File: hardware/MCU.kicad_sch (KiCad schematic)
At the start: 57 parts, among them SW2 SW_Push, SW3 SW_Push, U6 W25N02KVZEIR, Y1 Crystal, Y2 24MHz

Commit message: feat(Hw):Update_Schematic_And_BOM
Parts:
- added J2: Conn_01x04_Pin, Connector_PinHeader_2.54mm:PinHeader_1x04_P2.54mm_Vertical, symbol Connector:Conn_01x04_Pin
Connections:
- net +3V3: now also J2.4 (Pin_4)
- net DEBUG_RX: now also J2.2 (Pin_2)
- net DEBUG_TX: now also J2.3 (Pin_3)
- net GND: now also J2.1 (Pin_1)
- net CODEC_LINEOUT: no longer names the net of U8.29 (CODEC_LINEOUT)
- net CODEC_MIC0N: no longer names the net of U8.33 (CODEC_MIC0N)
- net CODEC_MIC0P: no longer names the net of U8.34 (CODEC_MIC0P)
- net CODEC_MIC1N: no longer names the net of U8.35 (CODEC_MIC1N)
- net CODEC_MIC1P: no longer names the net of U8.36 (CODEC_MIC1P)
- net CODEC_MICBIAS: no longer names the net of U8.32 (CODEC_MICBIAS)
- net CODEC_VCM: no longer names the net of C1.1, U8.30 (CODEC_VCM)
- net ETH_AVDD3V3: no longer names the net of R29.2, U8.101 (ETH_AVDD3V3)
- net ETH_PHY_RXN: no longer names the net of U8.97 (ETH_PHY_RXN)
- net ETH_PHY_RXP: no longer names the net of U8.98 (ETH_PHY_RXP)
- net ETH_PHY_TXN: no longer names the net of U8.99 (ETH_PHY_TXN)
- net ETH_PHY_TXP: no longer names the net of U8.100 (ETH_PHY_TXP)
- net GPIO0_A0_Z: no longer names the net of U8.58 (UART0_RX_M0/CLK_32K/CLK_REFOUT/RTC_CLKO/GPIO0_A0_Z)
- net GPIO0_A1_D: no longer names the net of U8.59 (UART0_TX_M0/PWM2_M0/GPIO0_A1_D)
- net GPIO0_A2_D: no longer names the net of U8.60 (PWM3_IR_M0/GPIO0_A2_D)
- net GPIO0_A3_U: no longer names the net of U8.62 (PMIC_PWR_CTRL_M1/GPIO0_A3_U)
- net GPIO0_A4_D: no longer names the net of U8.63 (PMIC_PWR_CTRL_M0/PWM1_M0/GPIO0_A4_D)
- net GPIO0_A5_D: no longer names the net of U8.64 (I2C1_SCL_M0/UART1_RTS_M0/PWM5_M0/GPIO0_A5_D)
- net GPIO0_A6_D: no longer names the net of U8.65 (I2C1_SDA_M0/UART1_CTS_M0/PWM6_M0/GPIO0_A6_D)
- net GPIO1_A2_D: no longer names the net of U8.74 (PWM0_M0/CPU_AVS/VI_CIF_D0_M1/GPIO1_A2_D)
- net GPIO1_A3_D: no longer names the net of U8.75 (UART1_TX_M0/I2C0_SCL_M0/GPIO1_A3_D)
- net GPIO1_A4_D: no longer names the net of U8.76 (UART1_RX_M0/I2C0_SDA_M0/GPIO1_A4_D)
- net GPIO1_B0_D: no longer names the net of U8.77 (UART4_RX_M0/PWM3_IR_M1/GPIO1_B0_D)
- net GPIO1_C1_D: no longer names the net of U8.94 (VO_LCDC_D6/VI_CIF_D3_M1/PWM4_M2/SPI0_CLK_M0/_SDMMC1_D0_M1/GPIO1_C1_D)
- net GPIO1_C3_D: no longer names the net of U8.92 (VO_LCDC_D4/VI_CIF_D5_M1/PWM6_M2/I2C4_SDA_M1/_SDMMC1_CMD_M1/SPI0_MISO_M0/GPIO1_C3_D)
- net GPIO1_C4_D: no longer names the net of U8.91 (VO_LCDC_D3/VI_CIF_D6_M1/PWM8_M1/UART4_RX_M1_/SDMMC1_D3_M1/GPIO1_C4_D)
- net GPIO1_C5_D: no longer names the net of U8.90 (VO_LCDC_D2/VI_CIF_D7_M1/PWM9_M1/UART4_TX_M1/_SDMMC1_D2_M1/GPIO1_C5_D)
- net GPIO1_C6_D: no longer names the net of U8.83 (VO_LCDC_D1/VI_CIF_D8_M1/PWM10_M1/UART4_RTS__M1/GPIO1_C6_D)
- net GPIO1_C7_D: no longer names the net of U8.84 (VO_LCDC_D0/VI_CIF_D9_M1/PWM11_IR_M1/UART4_CT_S_M1/GPIO1_C7_D)
- net GPIO1_D0_D: no longer names the net of U8.89 (VO_LCDC_DEN/VI_CIF_CLKI_M1/PWM3_IR_M2/UART5__RTS_M1/UART3_TX_M1/GPIO1_D0_D)
- net GPIO1_D1_D: no longer names the net of U8.87 (VO_LCDC_HSYNC/VI_CIF_HREF_M1/PWM10_M2/UART5__CTS_M1/UART3_RX_M1/GPIO1_D1_D)
- net GPIO1_D2_D: no longer names the net of U8.86 (VO_LCDC_VSYNC/VI_CIF_VSYNC_M1/I2C3_SDA_M1/UA_RT5_RX_M1/SPI0_CS1_M0/PWM0_M1/AUD_DSM_P/GPI_O1_D2_D)
- net GPIO1_D3_D: no longer names the net of U8.85 (VO_LCDC_CLK/VI_CIF_CLKO_M1/I2C3_SCL_M1/UART5__TX_M1/PWM11_IR_M2/AUD_DSM_N/GPIO1_D3_D)
- net GPIO2_A0_D_1: no longer names the net of U8.109 (SDMMC1_D1_M0/I2S0_SCLK/VO_LCDC_D8/UART1_CTS__M1/I2C4_SDA_M0/GPIO2_A0_D_1)
- net GPIO2_A0_D_2: no longer names the net of U8.110 (SDMMC1_D1_M0/I2S0_SCLK/VO_LCDC_D8/UART1_CTS__M1/I2C4_SDA_M0/GPIO2_A0_D_2)
- net GPIO2_A3_D: no longer names the net of U8.112 (SDMMC1_CMD_M0/I2S0_SDO3_SDI1/VO_LCDC_D11/GP_IO2_A3_D)
- net GPIO2_A4_D: no longer names the net of U8.113 (SDMMC1_D3_M0/I2S0_SDO0/VO_LCDC_D12/UART1_TX__M1/GPIO2_A4_D)
- net GPIO2_A5_D: no longer names the net of U8.114 (SDMMC1_D2_M0/I2S0_SDI0/VO_LCDC_D13/UART1_RX__M1/GPIO2_A5_D)
- net GPIO2_A6_D: no longer names the net of U8.107 (UART0_RTS_M1/I2S0_SDO2_SDI2/VO_LCDC_D14/PWM_2_M1/I2C3_SCL_M0/FLASH_TRIG_OUT/GPIO2_A6_D)
- net GPIO2_A7_D: no longer names the net of U8.106 (UART0_CTS_M1/I2S0_SDO1_SDI3/VO_LCDC_D15/PWM_4_M1/I2C3_SDA_M0/PRELIGHT_TRIG_OUT/GPIO2_A7_D)
- net GPIO2_A_2_D: no longer names the net of U8.111 (SDMMC1_CLK_M0/I2S0_MCLK/VO_LCDC_D10/GPIO2_A_2_D)
- net GPIO2_B1_D_1: no longer names the net of U8.104 (UART0_TX_M1/I2C1_SDA_M1/VO_LCDC_D17/PWM6_M1_/GPIO2_B1_D_1)
- net GPIO2_B1_D_2: no longer names the net of U8.105 (UART0_TX_M1/I2C1_SDA_M1/VO_LCDC_D17/PWM6_M1_/GPIO2_B1_D_2)
- net GPIO3_A3_U: no longer names the net of U8.14 (SDMMC0_D0/UART2_RX_M0/PWM8_M0/GPIO3_A3_U)
- net GPIO3_A4_D: no longer names the net of U8.15 (SDMMC0_CLK/UART5_RTS_M0/I2C0_SCL_M2/JTAG_LPMCU_TC_K_M1/PWM10_M0/GPIO3_A4_D)
- net GPIO3_A5_U: no longer names the net of U8.16 (SDMMC0_CMD/UART5_CTS_M0/I2C0_SDA_M2/JTAG_LPMCU_T_MS_M1/PWM11_IR_M0/GPIO3_A5_U)
- net GPIO3_A6_U: no longer names the net of U8.17 (SDMMC0_D3/UART5_TX_M0/JTAG_CPU_TMS_M0/JTAG_HPMCU__TMS_M1/GPIO3_A6_U)
- net GPIO3_A7_U: no longer names the net of U8.18 (SDMMC0_D2/UART5_RX_M0/JTAG_CPU_TCK_M0/JTAG_HPMCU__TCK_M1/GPIO3_A7_U)
- net GPIO3_B0_D: no longer names the net of U8.117 (VI_CIF_D0_M0/MIPI_CSI_RX_D3N/LVDS_RX_D3N/GPIO_3_B0_D)
- net GPIO3_B1_D: no longer names the net of U8.118 (VI_CIF_D1_M0/MIPI_CSI_RX_D3P/LVDS_RX_D3P/GPIO3__B1_D)
- net GPIO3_B2_D: no longer names the net of U8.119 (VI_CIF_D2_M0/MIPI_CSI_RX_CK1N/LVDS_RX_CK1N/GP_IO3_B2_D)
- net GPIO3_B3_D: no longer names the net of U8.120 (VI_CIF_D3_M0/MIPI_CSI_RX_CK1P/LVDS_RX_CK1P/GPI_O3_B3_D)
- net GPIO3_B4_D: no longer names the net of U8.121 (VI_CIF_D4_M0/MIPI_CSI_RX_D2N/LVDS_RX_D2N/GPIO_3_B4_D)
- net GPIO3_B5_D: no longer names the net of U8.122 (VI_CIF_D5_M0/MIPI_CSI_RX_D2P/LVDS_RX_D2P/GPIO3__B5_D)
- net GPIO3_B6_D renamed MCSI_D1N
- net GPIO3_B7_D renamed MCSI_D1P
- net GPIO3_C0_D renamed MCSI_CKN
- net GPIO3_C1_D renamed MCSI_CKP
- net GPIO3_C2_D renamed MCSI_D0N
- net GPIO3_C3_D renamed MCSI_D0P
- net GPIO3_C4_D renamed MCSI_MCLK
- net GPIO3_C5_D renamed MCSI_RST
- net GPIO3_C7_D renamed CSI_SCK
- net GPIO3_D0_D renamed CSI_SDA
- net GPIO3_D1_D: no longer names the net of U8.6 (VI_CIF_D13/UART5_RTS_M2/I2C3_SCL_M2/GPIO3_D1_D)
- net GPIO3_D2_D: no longer names the net of U8.8 (VI_CIF_D14/UART5_CTS_M2/I2C3_SDA_M2/GPIO3_D2_D)
- net GPIO3_D3_D: no longer names the net of U8.9 (VI_CIF_D15/PWM1_M2/GPIO3_D3_D)
- net GPIO4_A0_U: no longer names the net of U8.46 (EMMC_D7/SPI1_MISO_M0/UART0_RX_M2/I2C0_SDA_M1/GPIO_4_A0_U)
- net GPIO4_A1_U: no longer names the net of U8.45 (EMMC_D6/SPI1_MOSI_M0/UART0_TX_M2/I2C0_SCL_M1/GPIO_4_A1_U)
- net GPIO4_A5_U: no longer names the net of U8.40 (EMMC_D4/SPI1_CS0_M0/UART1_TX_M2/I2C2_SDA_M1/GPIO4__A5_U)
- net GPIO4_A7_U: no longer names the net of U8.38 (EMMC_D5/SPI1_CLK_M0/UART1_RX_M2/I2C2_SCL_M1/GPIO4__A7_U)
- no-connect marks 0 -> 59

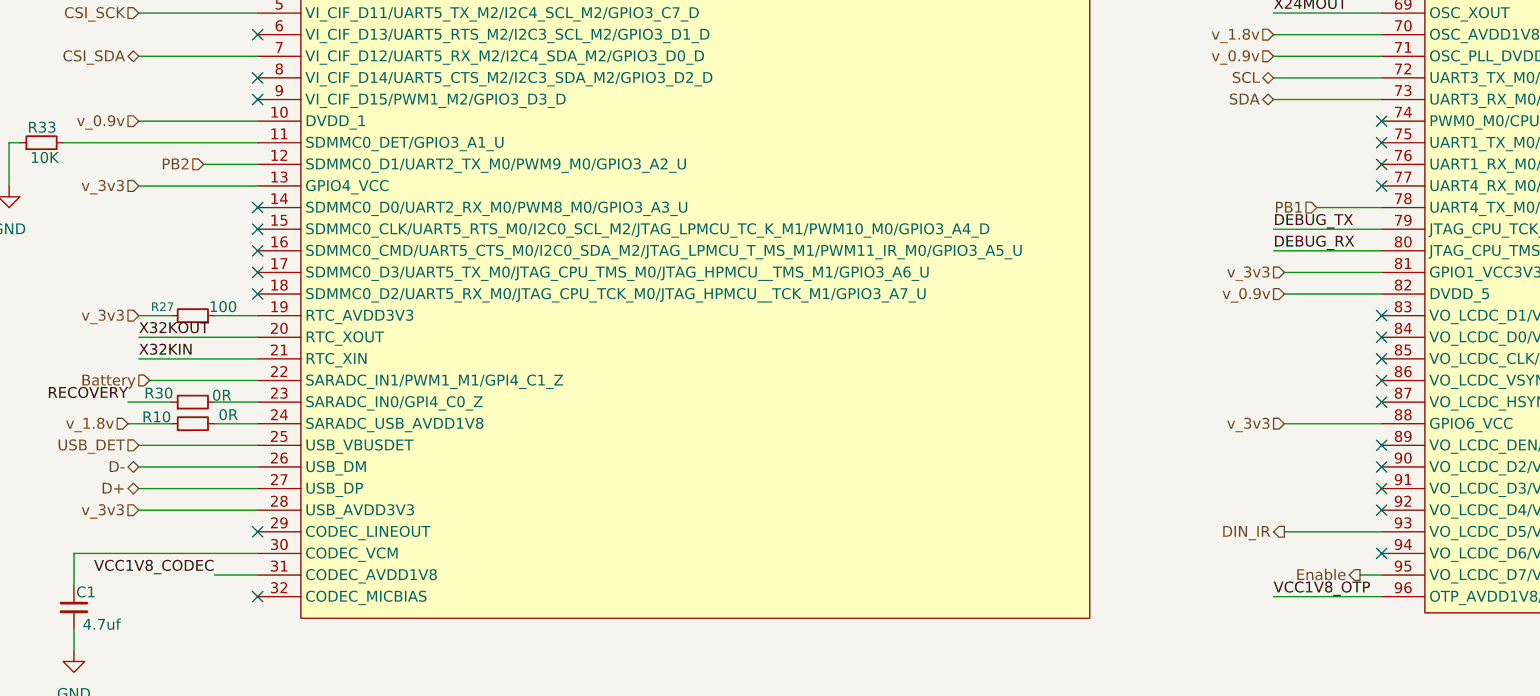
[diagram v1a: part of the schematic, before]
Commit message: feat(Hw):Update_Schematic_And_Floorplan
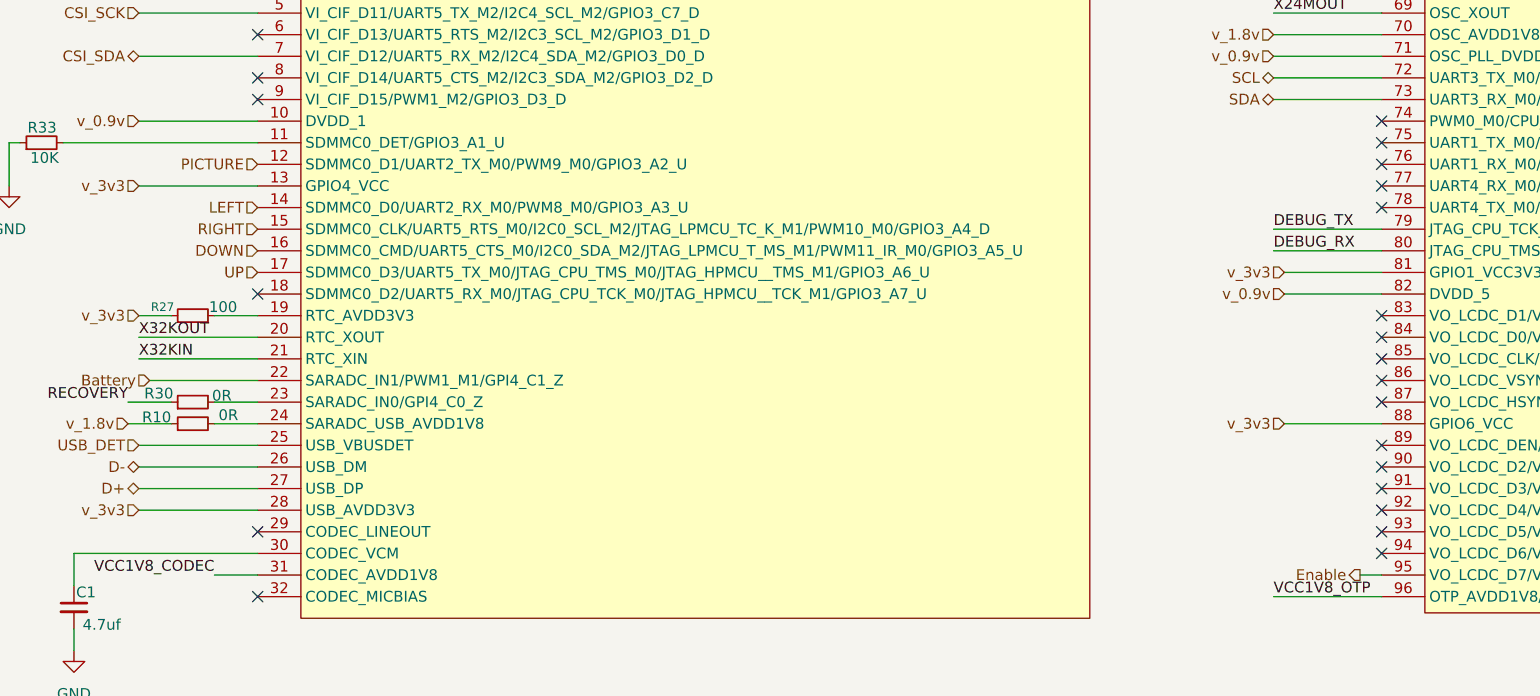
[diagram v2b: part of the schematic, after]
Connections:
- net LEFT: now reaches U8.14 (SDMMC0_D0/UART2_RX_M0/PWM8_M0/GPIO3_A3_U)
- net RIGHT: now reaches U8.15 (SDMMC0_CLK/UART5_RTS_M0/I2C0_SCL_M2/JTAG_LPMCU_TC_K_M1/PWM10_M0/GPIO3_A4_D)
- net DOWN: now reaches U8.16 (SDMMC0_CMD/UART5_CTS_M0/I2C0_SDA_M2/JTAG_LPMCU_T_MS_M1/PWM11_IR_M0/GPIO3_A5_U)
- net UP: now reaches U8.17 (SDMMC0_D3/UART5_TX_M0/JTAG_CPU_TMS_M0/JTAG_HPMCU__TMS_M1/GPIO3_A6_U)
- net DIN_IR: no longer names the net of U8.93 (VO_LCDC_D5/VI_CIF_D4_M1/PWM5_M2/I2C4_SCL_M1/_SDMMC1_CLK_M1/SPI0_MOSI_M0/GPIO1_C2_D)
- net PB1: no longer names the net of U8.78 (UART4_TX_M0/PWM7_IR_M1/SPI1_CS1_M0/VI_CIF_D1__M1/GPIO1_B1_D)
- net PB2 renamed PICTURE
- no-connect marks 59 -> 57
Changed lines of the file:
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@@
 	)
 	(no_connect
+		(at 285.75 91.44)
+	)
+	(no_connect
 		(at 153.67 38.1)
 	)
@@
 	)
 	(no_connect
-		(at 153.67 53.34)
-	)
-	(no_connect
 		(at 289.56 156.21)
 	)
@@
 	)
 	(no_connect
-		(at 153.67 55.88)
-	)
-	(no_connect
 		(at 285.75 68.58)
 	)
 	(no_connect
-		(at 153.67 58.42)
-	)
-	(no_connect
 		(at 285.75 81.28)
 	)
@@
 	)
 	(no_connect
+		(at 285.75 53.34)
+	)
+	(no_connect
 		(at 289.56 120.65)
 	)
@@
 	)
 	(no_connect
-		(at 153.67 60.96)
-	)
-	(no_connect
 		(at 289.56 128.27)
 	)
@@
 	(wire
 		(pts
-			(xy 274.32 91.44) (xy 285.75 91.44)
-		)
-		(stroke
-			(width 0)
-			(type default)
-		)
-	)
-	(wire
-		(pts
 			(xy 15.24 44.45) (xy 22.86 44.45)
 		)
@@
 	(wire
 		(pts
-			(xy 147.32 48.26) (xy 153.67 48.26)
-		)
-		(stroke
-			(width 0)
-			(type default)
-		)
-	)
-	(wire
-		(pts
 			(xy 20.32 78.74) (xy 20.32 80.01)
 		)
@@
 	(wire
 		(pts
-			(xy 278.13 53.34) (xy 285.75 53.34)
-		)
-		(stroke
-			(width 0)
-			(type default)
-		)
-	)
-	(wire
-		(pts
 			(xy 53.34 77.47) (xy 53.34 80.01)
 		)
@@
 		)
 	)
-	(hierarchical_label "DIN_IR"
-		(shape output)
-		(at 274.32 91.44 180)
+	(hierarchical_label "VCC_DDR"
+		(shape input)
+		(at 13.97 68.58 0)
 		(effects
 			(font
 				(size 1.27 1.27)
 			)
-			(justify right)
+			(justify left)
 		)
 	)
 	(hierarchical_label "VCC_DDR"
 		(shape input)
-		(at 13.97 68.58 0)
+		(at 153.67 160.02 180)
 		(effects
 			(font
 				(size 1.27 1.27)
 			)
-			(justify left)
+			(justify right)
 		)
 	)
-	(hierarchical_label "VCC_DDR"
+	(hierarchical_label "RIGHT"
 		(shape input)
-		(at 153.67 160.02 180)
+		(at 153.67 55.88 180)
 		(effects
 			(font
@@
 		)
 	)
+	(hierarchical_label "PICTURE"
+		(shape input)
+		(at 153.67 48.26 180)
+		(effects
+			(font
+				(size 1.27 1.27)
+			)
+			(justify right)
+		)
+	)
 	(hierarchical_label "v_0.9v"
 		(shape input)
@@
 		)
 	)
-	(hierarchical_label "PB2"
-		(shape input)
-		(at 147.32 48.26 180)
-		(effects
-			(font
-				(size 1.27 1.27)
-			)
-			(justify right)
-		)
-	)
 	(hierarchical_label "v_3v3"
 		(shape input)
@@
 		)
 	)
+	(hierarchical_label "UP"
+		(shape input)
+		(at 153.67 60.96 180)
+		(effects
+			(font
+				(size 1.27 1.27)
+			)
+			(justify right)
+		)
+	)
 	(hierarchical_label "VCC_DDR"
 		(shape input)
@@
 		)
 	)
-	(hierarchical_label "PB1"
+	(hierarchical_label "v_0.9v"
 		(shape input)
-		(at 278.13 53.34 180)
+		(at 153.67 165.1 180)
 		(effects
 			(font
@@
 		)
 	)
-	(hierarchical_label "v_0.9v"
+	(hierarchical_label "LEFT"
 		(shape input)
-		(at 153.67 165.1 180)
+		(at 153.67 53.34 180)
 		(effects
 			(font
@@
 		(effects
 			(font
+				(size 1.27 1.27)
+			)
+			(justify right)
+		)
+	)
+	(hierarchical_label "DOWN"
+		(shape input)
+		(at 153.67 58.42 180)
+		(effects
+			(font

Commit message: feat(Hw):Update_Schematic
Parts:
- removed R10, R28, R30: 0R, Resistor_SMD:R_0402_1005Metric, symbol Device:R_Small
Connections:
- net VDD_ARM is gone; now on net v_0.9v: C48.1, C49.1, U8.115 (CPU_DVDD)
- net +1V8: now also U8.24 (SARADC_USB_AVDD1V8)
- net RECOVERY: now also U8.23 (SARADC_IN0/GPI4_C0_Z)

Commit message: feat(Hw):Update_Schematic_And_BOM
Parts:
- D1: LCSC# C375573 -> C22371297
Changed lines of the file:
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@@
 			)
 		)
-		(property "LCSC#" "C375573"
+		(property "LCSC#" "C22371297"
 			(at 55.88 27.94 0)
 			(effects

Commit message: feat(Hw):Update_Floorplan_And_Route
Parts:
- J2: footprint Connector_PinHeader_2.54mm:PinHeader_1x04_P2.54mm_Vertical -> Footprints:4 Pin 2.54mm
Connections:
- net DOWN: now also U8.107 (UART0_RTS_M1/I2S0_SDO2_SDI2/VO_LCDC_D14/PWM_2_M1/I2C3_SCL_M0/FLASH_TRIG_OUT/GPIO2_A6_D); no longer U8.16 (SDMMC0_CMD/UART5_CTS_M0/I2C0_SDA_M2/JTAG_LPMCU_T_MS_M1/PWM11_IR_M0/GPIO3_A5_U)
- net LEFT: now also U8.106 (UART0_CTS_M1/I2S0_SDO1_SDI3/VO_LCDC_D15/PWM_4_M1/I2C3_SDA_M0/PRELIGHT_TRIG_OUT/GPIO2_A7_D); no longer U8.14 (SDMMC0_D0/UART2_RX_M0/PWM8_M0/GPIO3_A3_U)
- net PICTURE: now also U8.85 (VO_LCDC_CLK/VI_CIF_CLKO_M1/I2C3_SCL_M1/UART5__TX_M1/PWM11_IR_M2/AUD_DSM_N/GPIO1_D3_D); no longer U8.12 (SDMMC0_D1/UART2_TX_M0/PWM9_M0/GPIO3_A2_U)
- net RIGHT: now also U8.105 (UART0_TX_M1/I2C1_SDA_M1/VO_LCDC_D17/PWM6_M1_/GPIO2_B1_D_2); no longer U8.15 (SDMMC0_CLK/UART5_RTS_M0/I2C0_SCL_M2/JTAG_LPMCU_TC_K_M1/PWM10_M0/GPIO3_A4_D)
- net UP: now also U8.104 (UART0_TX_M1/I2C1_SDA_M1/VO_LCDC_D17/PWM6_M1_/GPIO2_B1_D_1); no longer U8.17 (SDMMC0_D3/UART5_TX_M0/JTAG_CPU_TMS_M0/JTAG_HPMCU__TMS_M1/GPIO3_A6_U)
- net DIN_IR: now reaches U8.93 (VO_LCDC_D5/VI_CIF_D4_M1/PWM5_M2/I2C4_SCL_M1/_SDMMC1_CLK_M1/SPI0_MOSI_M0/GPIO1_C2_D)
- no-connect marks 57 -> 56
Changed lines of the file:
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@@
 	)
 	(no_connect
-		(at 285.75 91.44)
+		(at 153.67 53.34)
 	)
 	(no_connect
@@
 	)
 	(no_connect
-		(at 153.67 63.5)
-	)
-	(no_connect
 		(at 285.75 76.2)
 	)
@@
 	)
 	(no_connect
+		(at 153.67 63.5)
+	)
+	(no_connect
 		(at 285.75 81.28)
 	)
 	(no_connect
+		(at 153.67 55.88)
+	)
+	(no_connect
 		(at 153.67 40.64)
 	)
@@
 	)
 	(no_connect
-		(at 285.75 20.32)
+		(at 153.67 58.42)
 	)
 	(no_connect
-		(at 289.56 181.61)
+		(at 285.75 20.32)
 	)
 	(no_connect
-		(at 289.56 146.05)
+		(at 289.56 181.61)
 	)
 	(no_connect
@@
 	)
 	(no_connect
-		(at 289.56 138.43)
+		(at 153.67 48.26)
 	)
 	(no_connect
@@
 	)
 	(no_connect
-		(at 289.56 143.51)
-	)
-	(no_connect
 		(at 285.75 93.98)
 	)
@@
 	)
 	(no_connect
-		(at 289.56 140.97)
-	)
-	(no_connect
 		(at 289.56 179.07)
 	)
@@
 	)
 	(no_connect
-		(at 285.75 71.12)
+		(at 153.67 60.96)
 	)
 	(no_connect
@@
 	(wire
 		(pts
+			(xy 276.86 138.43) (xy 289.56 138.43)
+		)
+		(stroke
+			(width 0)
+			(type default)
+		)
+	)
+	(wire
+		(pts
 			(xy 222.25 264.16) (xy 219.71 264.16)
 		)
@@
 	(wire
 		(pts
-			(xy 283.21 96.52) (xy 285.75 96.52)
+			(xy 280.67 96.52) (xy 285.75 96.52)
 		)
 		(stroke
@@
 	(wire
 		(pts
+			(xy 276.86 146.05) (xy 289.56 146.05)
+		)
+		(stroke
+			(width 0)
+			(type default)
+		)
+	)
+	(wire
+		(pts
 			(xy 22.86 173.99) (xy 22.86 176.53)
 		)
@@
 	(wire
 		(pts
+			(xy 276.86 140.97) (xy 289.56 140.97)
+		)
+		(stroke
+			(width 0)
+			(type default)
+		)
+	)
+	(wire
+		(pts
 			(xy 13.97 78.74) (xy 13.97 80.01)
 		)
@@
 	(wire
 		(pts
+			(xy 280.67 91.44) (xy 285.75 91.44)
+		)
+		(stroke
+			(width 0)
+			(type default)
+		)
+	)
+	(wire
+		(pts
 			(xy 261.62 133.35) (xy 289.56 133.35)
 		)
@@
 	(wire
 		(pts
+			(xy 274.32 71.12) (xy 285.75 71.12)
+		)
+		(stroke
+			(width 0)
+			(type default)
+		)
+	)
+	(wire
+		(pts
 			(xy 64.77 133.35) (xy 64.77 137.16)
 		)
@@
 	(wire
 		(pts
+			(xy 276.86 143.51) (xy 289.56 143.51)
+		)
+		(stroke
+			(width 0)
+			(type default)
+		)
+	)
+	(wire
+		(pts
 			(xy 63.5 185.42) (xy 63.5 190.5)
 		)
@@
 		)
 	)
+	(hierarchical_label "DIN_IR"
+		(shape output)
+		(at 280.67 91.44 180)
+		(effects
+			(font
+				(size 1.27 1.27)
+			)
+			(justify right)
+		)
+	)
 	(hierarchical_label "VCC_DDR"
 		(shape input)
@@
 	(hierarchical_label "RIGHT"
 		(shape input)
-		(at 153.67 55.88 180)
+		(at 276.86 140.97 180)
 		(effects
 			(font
@@
 	(hierarchical_label "PICTURE"
 		(shape input)
-		(at 153.67 48.26 180)
+		(at 274.32 71.12 180)
 		(effects
 			(font
@@
 	(hierarchical_label "Enable"
 		(shape output)
-		(at 283.21 96.52 180)
+		(at 280.67 96.52 180)
 		(effects
 			(font
@@
 	(hierarchical_label "UP"
 		(shape input)
-		(at 153.67 60.96 180)
+		(at 276.86 138.43 180)
 		(effects
 			(font
@@
 	(hierarchical_label "LEFT"
 		(shape input)
-		(at 153.67 53.34 180)
+		(at 276.86 143.51 180)
 		(effects
 			(font
@@
 	(hierarchical_label "DOWN"
 		(shape input)
-		(at 153.67 58.42 180)
+		(at 276.86 146.05 180)
 		(effects
 			(font
@@
 			)
 		)
-		(property "Footprint" "Connector_PinHeader_2.54mm:PinHeader_1x04_P2.54mm_Vertical"
+		(property "Footprint" "Footprints:4 Pin 2.54mm"
 			(at 102.87 260.35 0)
 			(effects

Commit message: feat(Hw):Update_3Dmodels_And_Rear_Board
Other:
- company: (none) -> Electronic Cats
- title: (none) -> Badge-HackGDL-2026
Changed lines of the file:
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@@
 	(generator_version "9.0")
 	(paper "A3")
+	(title_block
+		(title "Badge-HackGDL-2026")
+		(date "2026-01-15")
+		(rev "v1.0")
+		(company "Electronic Cats")
+		(comment 1 "Lizeth Gallegos Martínez")
+	)
 	(text "FLASH\n"
 		(exclude_from_sim no)
